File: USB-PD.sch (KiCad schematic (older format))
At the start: 32 parts, among them J11 E8124-015-01, Q7 SQS401EN-T1_BE3, U12 STUSB4500QTR

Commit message: Connected USB-PD and power select chip
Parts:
- added C153: C_100u_0805, antmicro-footprints:0805-cap, symbol antmicroCapacitorsmisc:C_100u_0805
- added C154: C_2u2_0402, sc606-baseboard-footprints:0402-cap, symbol sc606-baseboard:C_2u2_0402
- added C155: C_1u_0402, sc606-baseboard-footprints:0402-cap, symbol sc606-baseboard:C_1u_0402
- added IC3: TPS7A0518PDBVT, sc606-baseboard-footprints:SOT-23-5, symbol sc606-baseboard:TPS7A0518PDBVT
- added J1: PJ-202A, sc606-baseboard-footprints:Barrel_Jack_5.5mmODx2.1mmID_PJ-202A, symbol sc606-baseboard:PJ-202A
- added Q10: BSS84, antmicro-footprints:SOT-23-3, symbol antmicroTransistorsFETsMOSFETsSingle:BSS84
- added Q11: Si7223DN, sa800u-baseboard-hw-footprints:PowerPak-1212, symbol sa800u-baseboard-hw:Si7223DN
- added R161: R_220k_0402, antmicro-footprints:0402-res, symbol antmicroResistors0402:R_220k_0402
- added R163: R_24k9_0402, antmicro-footprints:0402-res, symbol antmicroResistors0402:R_24k9_0402
- added R164: R_180k_0402, antmicro-footprints:0402-res, symbol antmicroResistors0402:R_180k_0402
- added U14: LTC4416IMS-1, antmicro-footprints:MSOP-10_MS, symbol antmicroPMICPowerDistributionSwitchesLoadDrivers:LTC4416IMS-1
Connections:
- net labels added: AUX_VDD, VDD
- wire segments 134 -> 192
- no-connect marks 16 -> 17
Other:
- note added: "5-15V, lower priority"
- note added: "9...36 VDC"
- note added: "Auxiliary Power Control"
- note added: "Power input"
- note added: "USB-C PD"
- note added: "sprawdzić czy poprawny tranzystor"
- note added: "sprawdzić jaka ma byc dioda"
- moved on the sheet: C144, C145, C146, C152, C83, C84, D34, D7, D8, J12, Q9, R142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

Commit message: Changed barrel jack model, added power path controller
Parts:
- removed J1: PJ-202A, sc606-baseboard-footprints:Barrel_Jack_5.5mmODx2.1mmID_PJ-202A, symbol sc606-baseboard:PJ-202A
- removed Q10: BSS84, antmicro-footprints:SOT-23-3, symbol antmicroTransistorsFETsMOSFETsSingle:BSS84
- removed R161: R_220k_0402, antmicro-footprints:0402-res, symbol antmicroResistors0402:R_220k_0402
- removed R163: R_24k9_0402, antmicro-footprints:0402-res, symbol antmicroResistors0402:R_24k9_0402
- removed R164: R_180k_0402, antmicro-footprints:0402-res, symbol antmicroResistors0402:R_180k_0402
- removed U14: LTC4416IMS-1, antmicro-footprints:MSOP-10_MS, symbol antmicroPMICPowerDistributionSwitchesLoadDrivers:LTC4416IMS-1
- added C156, C157, C159: C_100n_0402, antmicro-footprints:0402-cap, symbol antmicroCapacitors0402:C_100n_0402
- added C158: C_1n_0402, antmicro-footprints:0402-res, symbol antmicroCapacitors0402:C_1n_0402
- added D36, D37: KP-1608EC, sc606-baseboard-footprints:LED_0603, symbol sc606-baseboard:KP-1608EC
- added J1: 1053131102, antmicro-footprints:1053131102, symbol antmicroRectangularConnectorsHeadersFemalePins:1053131102
- added Q10: Si7223DN, sc606-baseboard-footprints:PowerPak-1212, symbol sc606-baseboard:Si7223DN
- added R161, R165: R_768k_0402, antmicro-footprints:0402-res, symbol antmicroResistors0402:R_768k_0402
- added R163, R166: R_97k6_0402, antmicro-footprints:0402-res, symbol antmicroResistors0402:R_97k6_0402
- added R164, R167: R_30k1_0603, antmicro-footprints:0603-res, symbol antmicroResistors0603:R_30k1_0603
- added R168, R169: R_270R_0603, antmicro-footprints:0603-res, symbol antmicroResistors0603:R_270R_0603
- added U14: LTC4418IUF#PBF, antmicro-footprints:QFN-20_1EP_4x4_P0.5mm, symbol antmicroPMICPowerDistributionSwitchesLoadDrivers:LTC4418IUF#PBF
- C153: footprint antmicro-footprints:0805-cap -> sc606-baseboard-footprints:0805-cap; symbol antmicroCapacitorsmisc:C_100u_0805 -> sc606-baseboard:C_100u_0805
- Q11: footprint sa800u-baseboard-hw-footprints:PowerPak-1212 -> sc606-baseboard-footprints:PowerPak-1212; symbol sa800u-baseboard-hw:Si7223DN -> sc606-baseboard:Si7223DN
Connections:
- wire segments 192 -> 220
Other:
- note added: "5-20V, lower priority"
- note removed: "5-15V, lower priority"

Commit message: Adjusted position of uHDMI
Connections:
- wire segments 220 -> 221
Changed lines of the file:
@@
 	8125 8200 6675 8200
 Connection ~ 6675 8200
+Wire Wire Line
+	6475 6525 6575 6525
+Connection ~ 6575 6525
 $EndSCHEMATC

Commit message: Changed ESD diode and transistor near USB-PD
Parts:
- removed D35: ESD144B1W0201E6327XTSA1, sc606-baseboard-footprints:ESD144B1W0201E6327XTSA1, symbol sc606-baseboard:ESD144B1W0201E6327XTSA1
- removed Q7: SQS401EN-T1_BE3, sc606-baseboard-footprints:Vishay_PowerPAK_1212-8_Single, symbol sc606-baseboard:SQS401EN-T1_BE3
- added D35: PESD18VF1BSFYL, antmicro-footprints:RESC0603X26N, symbol antmicroTVSDiodes:PESD18VF1BSFYL
- added Q9: SQS401EN-T1_BE3, antmicro-footprints:Vishay_PowerPAK_1212-8_Single, symbol antmicroTransistorsFETsMOSFETsSingle:SQS401EN-T1_BE3
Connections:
- wire segments 221 -> 222
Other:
- note added: "9-20V, higher priority"
- note added: "9-20V, lower priority"
- note added: "9...20 VDC"
- note removed: "5-20V, lower priority"
- note removed: "9...36 VDC"
- note removed: "sprawdzić jaka ma byc dioda"
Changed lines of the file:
@@
 	10000 1300 10000 1600
-Wire Wire Line
-	9500 1600 9000 1600
 Wire Wire Line
 	10600 900  10600 1100
@@
 NoConn ~ 3750 1200
 NoConn ~ 3750 1300
-$Comp
-L sc606-baseboard:ESD144B1W0201E6327XTSA1 D35
-U 1 1 630E4F56
-P 11450 1250
-F 0 "D35" V 11404 1328 50  0000 L CNN
-F 1 "ESD144B1W0201E6327XTSA1" V 11495 1328 50  0000 L CNN
-F 2 "sc606-baseboard-footprints:ESD144B1W0201E6327XTSA1" H 11450 1250 50  0001 C CNN
-F 3 "https://www.infineon.com/dgdl/Infineon-ESD144-B1-W0201-DataSheet-v02_00-EN.pdf?fileId=5546d462677d0f4601679886a2a8707c" H 11450 1250 50  0001 C CNN
-F 4 "ESD144B1W0201E6327XTSA1" H 11450 1250 50  0001 C CNN "MPN"
-F 5 "Infineon Technologies" H 11450 1250 50  0001 C CNN "Manufacturer"
-	1    11450 1250
-	0    1    1    0
-$EndComp
 Wire Wire Line
 	11450 1600 11450 1650
@@
 	1    0    0    -1
 $EndComp
-$Comp
-L sc606-baseboard:SQS401EN-T1_BE3 Q?
-U 1 1 62135D7B
-P 8900 900
-AR Path="/61B0DC30/62135D7B" Ref="Q?"  Part="1"
-AR Path="/61DF77CE/62135D7B" Ref="Q7"  Part="1"
-AR Path="/623AED4D/62135D7B" Ref="Q9"  Part="1"
-F 0 "Q9" V 9167 900 60  0000 C CNN
-F 1 "SQS401EN-T1_BE3" V 9061 900 60  0000 C CNN
-F 2 "sc606-baseboard-footprints:Vishay_PowerPAK_1212-8_Single" H 9100 1100 60  0001 L CNN
-F 3 "https://www.vishay.com/docs/65529/sqs401en.pdf" H 9100 1200 60  0001 L CNN
-F 4 "SQS401EN-T1_BE3" H 9100 1400 60  0001 L CNN "MPN"
-F 5 "Vishay" H 9100 2000 60  0001 L CNN "Manufacturer"
-	1    8900 900
-	0    -1   -1   0
-$EndComp
 Wire Wire Line
 	9100 900  10000 900
 Wire Wire Line
-	9000 1200 9000 1600
-Connection ~ 9000 1600
-Wire Wire Line
-	7450 1600 9000 1600
+	8800 1200 8800 1600
+Wire Wire Line
+	7450 1600 8800 1600
 Wire Wire Line
 	7450 900  8700 900
@@
 	4950 3450 4950 3750
 NoConn ~ 4750 3750
-Wire Wire Line
-	11050 900  11450 900
 $Comp
 L sc606-baseboard:GND #PWR0177
@@
 Wire Wire Line
 	2550 2200 2550 2350
-Connection ~ 11450 900
-Wire Wire Line
-	11450 900  11900 900
-Text Notes 4850 8300 0    50   ~ 0
-5-20V, lower priority
+Text Notes 6850 7000 0    50   ~ 0
+9-20V, lower priority
 Wire Wire Line
 	10525 7150 10525 7100
@@
 AUX_VDD
 Text Notes 2750 7300 0    50   ~ 0
-9...36 VDC
+9...20 VDC
 Text Notes 7200 6050 0    100  ~ 20
 Auxiliary Power Control
 Text Notes 9400 750  0    50   ~ 0
 sprawdzić czy poprawny tranzystor
-Text Notes 11850 1500 0    50   ~ 0
-sprawdzić jaka ma byc dioda
 $Comp
 L sc606-baseboard:C_100u_0805 C153
@@
 	6475 6525 6575 6525
 Connection ~ 6575 6525
+Text Notes 4775 6700 0    50   ~ 0
+9-20V, higher priority
+Text Notes 11925 1050 0    50   ~ 0
+9...20 VDC
+$Comp
+L antmicroTransistorsFETsMOSFETsSingle:SQS401EN-T1_BE3 Q9
+U 1 1 6267FF4C
+P 8900 900
+F 0 "Q9" V 9167 900 60  0000 C CNN
+F 1 "SQS401EN-T1_BE3" V 9061 900 60  0000 C CNN
+F 2 "antmicro-footprints:Vishay_PowerPAK_1212-8_Single" H 9100 1100 60  0001 L CNN
+F 3 "https://www.vishay.com/docs/65529/sqs401en.pdf" H 9100 1200 60  0001 L CNN
+F 4 "SQS401EN-T1_BE3" H 9100 1400 60  0001 L CNN "MPN"
+F 5 "Vishay" H 9100 2000 60  0001 L CNN "Manufacturer"
+	1    8900 900
+	0    1    -1   0
+$EndComp
+Connection ~ 8800 1600
+Wire Wire Line
+	8800 1600 9500 1600
+$Comp
+L antmicroTVSDiodes:PESD18VF1BSFYL D35
+U 1 1 626DCF07
+P 11450 1350
+F 0 "D35" V 11379 1453 100 0000 L CNN
+F 1 "PESD18VF1BSFYL" V 11545 1453 100 0000 L CNN
+F 2 "antmicro-footprints:RESC0603X26N" H 11450 900 100 0001 L CNN
+F 3 "https://www.mouser.pl/datasheet/2/916/PESD18VF1BSF-1599696.pdf" H 11660 1200 100 0001 C CNN
+F 4 "nexperia" H 11450 775 100 0001 L CNN "Manufacturer"
+F 5 "PESD18VF1BSFYL" H 11450 1025 100 0001 L CNN "MPN"
+	1    11450 1350
+	0    1    1    0
+$EndComp
+Wire Wire Line
+	11050 900  11450 900
+Wire Wire Line
+	11450 900  11450 1125
+Connection ~ 11450 900
+Wire Wire Line
+	11450 900  11900 900
 $EndSCHEMATC

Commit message: Connected differential signals from camera modules and LCD display. Without checking track lengths
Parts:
- C156, C157, C159: footprint antmicro-footprints:0402-cap -> sc606-baseboard-footprints:0402-cap; symbol antmicroCapacitors0402:C_100n_0402 -> sc606-baseboard:C_100n_0402
- C158: footprint antmicro-footprints:0402-res -> sc606-baseboard-footprints:0402-res; symbol antmicroCapacitors0402:C_1n_0402 -> sc606-baseboard:C_1n_0402
- D35: footprint antmicro-footprints:RESC0603X26N -> sc606-baseboard-footprints:RESC0603X26N; symbol antmicroTVSDiodes:PESD18VF1BSFYL -> sc606-baseboard:PESD18VF1BSFYL
- J1: footprint antmicro-footprints:1053131102 -> sc606-baseboard-footprints:1053131102; symbol antmicroRectangularConnectorsHeadersFemalePins:1053131102 -> sc606-baseboard:1053131102
- Q9: footprint antmicro-footprints:Vishay_PowerPAK_1212-8_Single -> sc606-baseboard-footprints:Vishay_PowerPAK_1212-8_Single; symbol antmicroTransistorsFETsMOSFETsSingle:SQS401EN-T1_BE3 -> sc606-baseboard:SQS401EN-T1_BE3
- R161, R165: footprint antmicro-footprints:0402-res -> sc606-baseboard-footprints:0402-res; symbol antmicroResistors0402:R_768k_0402 -> sc606-baseboard:R_768k_0402
- R163, R166: footprint antmicro-footprints:0402-res -> sc606-baseboard-footprints:0402-res; symbol antmicroResistors0402:R_97k6_0402 -> sc606-baseboard:R_97k6_0402
- R164, R167: footprint antmicro-footprints:0603-res -> sc606-baseboard-footprints:0603-res; symbol antmicroResistors0603:R_30k1_0603 -> sc606-baseboard:R_30k1_0603
- R168, R169: footprint antmicro-footprints:0603-res -> sc606-baseboard-footprints:0603-res; symbol antmicroResistors0603:R_270R_0603 -> sc606-baseboard:R_270R_0603
- U14: footprint antmicro-footprints:QFN-20_1EP_4x4_P0.5mm -> sc606-baseboard-footprints:QFN-20_1EP_4x4_P0.5mm; symbol antmicroPMICPowerDistributionSwitchesLoadDrivers:LTC4418IUF#PBF -> sc606-baseboard:LTC4418IUF#PBF
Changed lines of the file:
@@
 5V_SYS
 $Comp
-L antmicroRectangularConnectorsHeadersFemalePins:1053131102 J1
+L sc606-baseboard:1053131102 J1
 U 1 1 620288D5
 P 2250 7100
 F 0 "J1" H 2358 7265 50  0000 C CNN
 F 1 "1053131102" H 2358 7174 50  0000 C CNN
-F 2 "antmicro-footprints:1053131102" H 2075 6775 50  0001 C CNN
+F 2 "sc606-baseboard-footprints:1053131102" H 2075 6775 50  0001 C CNN
 F 3 "" H 2250 7100 50  0001 C CNN
 F 4 "Molex" H 2200 6575 50  0001 C CNN "Manufacturer"
@@
 $EndComp
 $Comp
-L antmicroPMICPowerDistributionSwitchesLoadDrivers:LTC4418IUF#PBF U14
+L sc606-baseboard:LTC4418IUF#PBF U14
 U 1 1 6207B24A
 P 8725 8600
 F 0 "U14" H 8725 9467 50  0000 C CNN
 F 1 "LTC4418IUF#PBF" H 8725 9376 50  0000 C CNN
-F 2 "antmicro-footprints:QFN-20_1EP_4x4_P0.5mm" H 8325 7600 50  0001 L BNN
+F 2 "sc606-baseboard-footprints:QFN-20_1EP_4x4_P0.5mm" H 8325 7600 50  0001 L BNN
 F 3 "https://www.analog.com/media/en/technical-documentation/data-sheets/ltc4418.pdf" H 8725 8600 50  0001 L BNN
 F 4 "AnalogDevices" H 8325 7550 50  0001 L BNN "MANUFACTURER"
@@
 $EndComp
 $Comp
-L antmicroCapacitors0402:C_100n_0402 C159
+L sc606-baseboard:C_100n_0402 C159
 U 1 1 62093795
 P 9800 8750
 F 0 "C159" H 9685 8705 60  0000 R CNN
 F 1 "C_100n_0402" H 9800 8600 60  0001 C CNN
-F 2 "antmicro-footprints:0402-cap" H 10000 8950 60  0001 L CNN
+F 2 "sc606-baseboard-footprints:0402-cap" H 10000 8950 60  0001 L CNN
 F 3 "" H 9800 8750 50  0001 C CNN
 F 4 "Murata" H 10000 9150 60  0001 L CNN "Manufacturer"
@@
 $EndComp
 $Comp
-L antmicroCapacitors0402:C_1n_0402 C158
+L sc606-baseboard:C_1n_0402 C158
 U 1 1 62094A57
 P 9550 9400
 F 0 "C158" H 9665 9445 60  0000 L CNN
 F 1 "C_1n_0402" H 9550 9250 60  0001 C CNN
-F 2 "antmicro-footprints:0402-res" H 9750 9600 60  0001 L CNN
+F 2 "sc606-baseboard-footprints:0402-res" H 9750 9600 60  0001 L CNN
 F 3 "" H 9550 9400 50  0001 C CNN
 F 4 "YAGEO" H 9750 9800 60  0001 L CNN "Manufacturer"
@@
 NoConn ~ 9325 8400
 $Comp
-L antmicroCapacitors0402:C_100n_0402 C156
+L sc606-baseboard:C_100n_0402 C156
 U 1 1 620BEA75
 P 7525 9500
 F 0 "C156" H 7410 9455 60  0000 R CNN
 F 1 "C_100n_0402" H 7525 9350 60  0001 C CNN
-F 2 "antmicro-footprints:0402-cap" H 7725 9700 60  0001 L CNN
+F 2 "sc606-baseboard-footprints:0402-cap" H 7725 9700 60  0001 L CNN
 F 3 "" H 7525 9500 50  0001 C CNN
 F 4 "Murata" H 7725 9900 60  0001 L CNN "Manufacturer"
@@
 $EndComp
 $Comp
-L antmicroCapacitors0402:C_100n_0402 C157
+L sc606-baseboard:C_100n_0402 C157
 U 1 1 620BF040
 P 7800 9500
 F 0 "C157" H 7915 9455 60  0000 L CNN
 F 1 "C_100n_0402" H 7800 9350 60  0001 C CNN
-F 2 "antmicro-footprints:0402-cap" H 8000 9700 60  0001 L CNN
+F 2 "sc606-baseboard-footprints:0402-cap" H 8000 9700 60  0001 L CNN
 F 3 "" H 7800 9500 50  0001 C CNN
 F 4 "Murata" H 8000 9900 60  0001 L CNN "Manufacturer"
@@
 $EndComp
 $Comp
-L antmicroResistors0603:R_270R_0603 R168
+L sc606-baseboard:R_270R_0603 R168
 U 1 1 6201E54F
 P 10500 8200
 F 0 "R168" H 10500 8413 60  0000 C CNN
 F 1 "R_270R_0603" H 10500 8050 60  0001 C CNN
-F 2 "antmicro-footprints:0603-res" H 10700 8400 60  0001 L CNN
+F 2 "sc606-baseboard-footprints:0603-res" H 10700 8400 60  0001 L CNN
 F 3 "https://industrial.panasonic.com/cdbs/www-data/pdf/RDA0000/AOA0000C304.pdf" H 10500 8200 50  0001 C CNN
 F 4 "Panasonic" H 10700 8600 60  0001 L CNN "Manufacturer"
@@
 $EndComp
 $Comp
-L antmicroResistors0603:R_270R_0603 R169
+L sc606-baseboard:R_270R_0603 R169
 U 1 1 6201EDA2
 P 10500 8300
 F 0 "R169" H 10500 8177 60  0000 C CNN
 F 1 "R_270R_0603" H 10500 8150 60  0001 C CNN
-F 2 "antmicro-footprints:0603-res" H 10700 8500 60  0001 L CNN
+F 2 "sc606-baseboard-footprints:0603-res" H 10700 8500 60  0001 L CNN
 F 3 "https://industrial.panasonic.com/cdbs/www-data/pdf/RDA0000/AOA0000C304.pdf" H 10500 8300 50  0001 C CNN
 F 4 "Panasonic" H 10700 8700 60  0001 L CNN "Manufacturer"
@@
 	8125 8900 6125 8900
 $Comp
-L antmicroResistors0402:R_97k6_0402 R166
+L sc606-baseboard:R_97k6_0402 R166
 U 1 1 621C7E01
 P 6925 8500
 F 0 "R166" H 7125 8500 60  0000 C CNN
 F 1 "R_97k6_0402" H 6925 8350 60  0001 C CNN
-F 2 "antmicro-footprints:0402-res" H 7125 8700 60  0001 L CNN
+F 2 "sc606-baseboard-footprints:0402-res" H 7125 8700 60  0001 L CNN
 F 3 "" H 6925 8500 50  0001 C CNN
 F 4 "MULTICOMP" H 7125 8900 60  0001 L CNN "Manufacturer"
@@
 $EndComp
 $Comp
-L antmicroResistors0603:R_30k1_0603 R167
+L sc606-baseboard:R_30k1_0603 R167
 U 1 1 621C29F0
 P 6925 8600
 F 0 "R167" H 6925 8525 60  0000 C CNN
 F 1 "R_30k1_0603" H 6925 8450 60  0001 C CNN
-F 2 "antmicro-footprints:0603-res" H 7125 8800 60  0001 L CNN
+F 2 "sc606-baseboard-footprints:0603-res" H 7125 8800 60  0001 L CNN
 F 3 "" H 6925 8600 50  0001 C CNN
 F 4 "VISHAY" H 7125 9000 60  0001 L CNN "Manufacturer"
@@
 $EndComp
 $Comp
-L antmicroResistors0402:R_768k_0402 R165
+L sc606-baseboard:R_768k_0402 R165
 U 1 1 62256146
 P 6925 8350
 F 0 "R165" H 6880 8420 60  0000 L CNN
 F 1 "R_768k_0402" H 6925 8200 60  0001 C CNN
-F 2 "antmicro-footprints:0402-res" H 7125 8550 60  0001 L CNN
+F 2 "sc606-baseboard-footprints:0402-res" H 7125 8550 60  0001 L CNN
 F 3 "" H 6925 8350 50  0001 C CNN
 F 4 "Vishay" H 7125 8750 60  0001 L CNN "Manufacturer"
@@
 	7225 6800 7875 6800
 $Comp
-L antmicroResistors0603:R_30k1_0603 R164
+L sc606-baseboard:R_30k1_0603 R164
 U 1 1 62390D9D
 P 6525 8200
 F 0 "R164" H 6525 8125 60  0000 C CNN
 F 1 "R_30k1_0603" H 6525 8050 60  0001 C CNN
-F 2 "antmicro-footprints:0603-res" H 6725 8400 60  0001 L CNN
+F 2 "sc606-baseboard-footprints:0603-res" H 6725 8400 60  0001 L CNN
 F 3 "" H 6525 8200 50  0001 C CNN
 F 4 "VISHAY" H 6725 8600 60  0001 L CNN "Manufacturer"
@@
 $EndComp
 $Comp
-L antmicroResistors0402:R_97k6_0402 R163
+L sc606-baseboard:R_97k6_0402 R163
 U 1 1 623917A8
 P 6525 8100
 F 0 "R163" H 6725 8100 60  0000 C CNN
 F 1 "R_97k6_0402" H 6525 7950 60  0001 C CNN
-F 2 "antmicro-footprints:0402-res" H 6725 8300 60  0001 L CNN
+F 2 "sc606-baseboard-footprints:0402-res" H 6725 8300 60  0001 L CNN
 F 3 "" H 6525 8100 50  0001 C CNN
 F 4 "MULTICOMP" H 6725 8500 60  0001 L CNN "Manufacturer"
@@
 	5775 7450 5775 6525
 $Comp
-L antmicroResistors0402:R_768k_0402 R161
+L sc606-baseboard:R_768k_0402 R161
 U 1 1 623B7E6A
 P 6525 7950
 F 0 "R161" H 6480 8020 60  0000 L CNN
 F 1 "R_768k_0402" H 6525 7800 60  0001 C CNN
-F 2 "antmicro-footprints:0402-res" H 6725 8150 60  0001 L CNN
+F 2 "sc606-baseboard-footprints:0402-res" H 6725 8150 60  0001 L CNN
 F 3 "" H 6525 7950 50  0001 C CNN
 F 4 "Vishay" H 6725 8350 60  0001 L CNN "Manufacturer"
@@
 9...20 VDC
 $Comp
-L antmicroTransistorsFETsMOSFETsSingle:SQS401EN-T1_BE3 Q9
+L sc606-baseboard:SQS401EN-T1_BE3 Q9
 U 1 1 6267FF4C
 P 8900 900
 F 0 "Q9" V 9167 900 60  0000 C CNN
 F 1 "SQS401EN-T1_BE3" V 9061 900 60  0000 C CNN
-F 2 "antmicro-footprints:Vishay_PowerPAK_1212-8_Single" H 9100 1100 60  0001 L CNN
+F 2 "sc606-baseboard-footprints:Vishay_PowerPAK_1212-8_Single" H 9100 1100 60  0001 L CNN
 F 3 "https://www.vishay.com/docs/65529/sqs401en.pdf" H 9100 1200 60  0001 L CNN
 F 4 "SQS401EN-T1_BE3" H 9100 1400 60  0001 L CNN "MPN"
@@
 	8800 1600 9500 1600
 $Comp
-L antmicroTVSDiodes:PESD18VF1BSFYL D35
+L sc606-baseboard:PESD18VF1BSFYL D35
 U 1 1 626DCF07
 P 11450 1350
 F 0 "D35" V 11379 1453 100 0000 L CNN
 F 1 "PESD18VF1BSFYL" V 11545 1453 100 0000 L CNN
-F 2 "antmicro-footprints:RESC0603X26N" H 11450 900 100 0001 L CNN
+F 2 "sc606-baseboard-footprints:RESC0603X26N" H 11450 900 100 0001 L CNN
 F 3 "https://www.mouser.pl/datasheet/2/916/PESD18VF1BSF-1599696.pdf" H 11660 1200 100 0001 C CNN
 F 4 "nexperia" H 11450 775 100 0001 L CNN "Manufacturer"

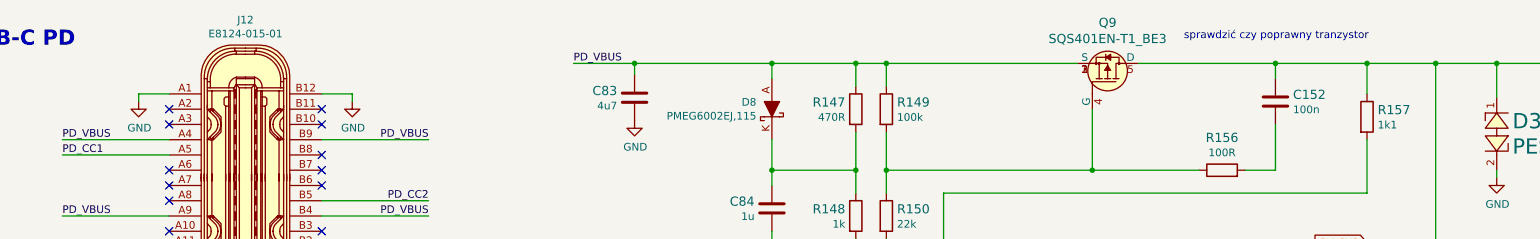
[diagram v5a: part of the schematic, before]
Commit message: Routed USB flash and both USB connectors differential signals with tuning
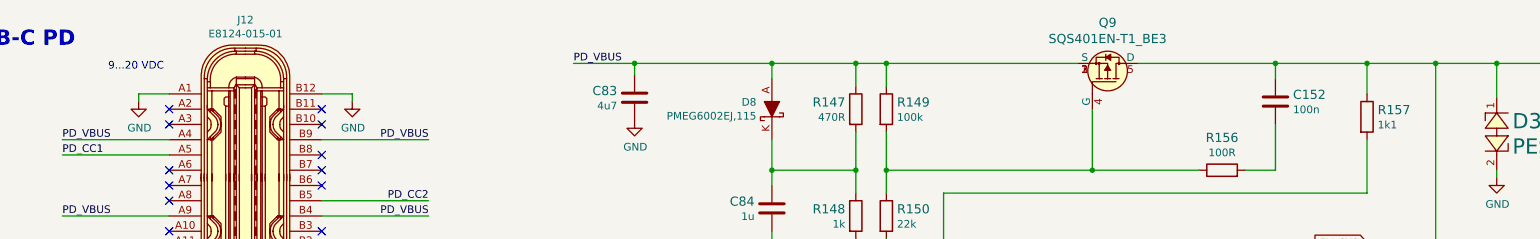
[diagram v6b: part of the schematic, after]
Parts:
- removed Q9: SQS401EN-T1_BE3, sc606-baseboard-footprints:Vishay_PowerPAK_1212-8_Single, symbol sc606-baseboard:SQS401EN-T1_BE3
- added Q9: SQS401EN-T1_BE3, antmicro-footprints:Vishay_PowerPAK_1212-8_Single, symbol antmicroTransistorsFETsMOSFETsSingle:SQS401EN-T1_BE3
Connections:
- net PD_VBUS: now also Q9.1 (S), Q9.2 (S), Q9.3 (S)
- net PD_VDD: now also Q9.5 (D)
- net at R149.2, R150.1, R156.1: now also Q9.4 (G)
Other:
- note removed: "sprawdzić czy poprawny tranzystor"
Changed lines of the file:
@@
 Text Notes 7200 6050 0    100  ~ 20
 Auxiliary Power Control
-Text Notes 9400 750  0    50   ~ 0
-sprawdzić czy poprawny tranzystor
 $Comp
 L sc606-baseboard:C_100u_0805 C153
@@
 Text Notes 11925 1050 0    50   ~ 0
 9...20 VDC
-$Comp
-L sc606-baseboard:SQS401EN-T1_BE3 Q9
-U 1 1 6267FF4C
-P 8900 900
-F 0 "Q9" V 9167 900 60  0000 C CNN
-F 1 "SQS401EN-T1_BE3" V 9061 900 60  0000 C CNN
-F 2 "sc606-baseboard-footprints:Vishay_PowerPAK_1212-8_Single" H 9100 1100 60  0001 L CNN
-F 3 "https://www.vishay.com/docs/65529/sqs401en.pdf" H 9100 1200 60  0001 L CNN
-F 4 "SQS401EN-T1_BE3" H 9100 1400 60  0001 L CNN "MPN"
-F 5 "Vishay" H 9100 2000 60  0001 L CNN "Manufacturer"
-	1    8900 900
-	0    1    -1   0
-$EndComp
 Connection ~ 8800 1600
 Wire Wire Line
@@
 Wire Wire Line
 	11450 900  11900 900
+$Comp
+L antmicroTransistorsFETsMOSFETsSingle:SQS401EN-T1_BE3 Q9
+U 1 1 620802FD
+P 8900 900
+F 0 "Q9" V 9167 900 60  0000 C CNN
+F 1 "SQS401EN-T1_BE3" V 9061 900 60  0000 C CNN
+F 2 "antmicro-footprints:Vishay_PowerPAK_1212-8_Single" H 9100 1100 60  0001 L CNN
+F 3 "https://www.vishay.com/docs/65529/sqs401en.pdf" H 9100 1200 60  0001 L CNN
+F 4 "SQS401EN-T1_BE3" H 9100 1400 60  0001 L CNN "MPN"
+F 5 "Vishay" H 9100 2000 60  0001 L CNN "Manufacturer"
+	1    8900 900
+	0    1    -1   0
+$EndComp
+Text Notes 2350 950  0    50   ~ 0
+9...20 VDC
 $EndSCHEMATC

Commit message: Connected SIM, SD, SoM GNDs
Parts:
- Q9: footprint antmicro-footprints:Vishay_PowerPAK_1212-8_Single -> sc606-baseboard-footprints:Vishay_PowerPAK_1212-8_Single; symbol antmicroTransistorsFETsMOSFETsSingle:SQS401EN-T1_BE3 -> sc606-baseboard:SQS401EN-T1_BE3
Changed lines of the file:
@@
 	11450 900  11900 900
 $Comp
-L antmicroTransistorsFETsMOSFETsSingle:SQS401EN-T1_BE3 Q9
+L sc606-baseboard:SQS401EN-T1_BE3 Q9
 U 1 1 620802FD
 P 8900 900
 F 0 "Q9" V 9167 900 60  0000 C CNN
 F 1 "SQS401EN-T1_BE3" V 9061 900 60  0000 C CNN
-F 2 "antmicro-footprints:Vishay_PowerPAK_1212-8_Single" H 9100 1100 60  0001 L CNN
+F 2 "sc606-baseboard-footprints:Vishay_PowerPAK_1212-8_Single" H 9100 1100 60  0001 L CNN
 F 3 "https://www.vishay.com/docs/65529/sqs401en.pdf" H 9100 1200 60  0001 L CNN
 F 4 "SQS401EN-T1_BE3" H 9100 1400 60  0001 L CNN "MPN"
